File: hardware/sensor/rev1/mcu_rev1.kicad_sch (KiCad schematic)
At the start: 21 parts, among them IC1 STM8L051F3P6, J1 22-28-4044, J2 M20-9770342

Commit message: EG-49 Takachi PCB format.
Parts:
- removed LED3: TLHR4400-AS12Z, MyParts:TLHR4400AS12Z, symbol TLHR4400-AS12Z:TLHR4400-AS12Z
- removed S1, S3: MASM-14R-8-10, MyParts:MASM14R810, symbol MASM-14R-8-10:MASM-14R-8-10
- removed S2: TL6120DF160QG, MyParts:TL6120DF160QG, symbol TL6120DF160QG:TL6120DF160QG
- added LED1: APTD1608LSURCK, MyParts:LEDM168X95N, symbol APTD1608LSURCK:APTD1608LSURCK
- added S1, S3: GP560_20-25, MyParts:GP5602025, symbol GP560_20-25:GP560_20-25
- added S2: PTS636SMG25JSMTR_LFS, MyParts:PTS636SMG25JSMTRLFS, symbol PTS636SMG25JSMTR_LFS:PTS636SMG25JSMTR_LFS
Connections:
- net BTN: now also S2.1 (COM)
- net GND: now also LED1.1 (K), S1.1, S2.2 (NO), S3.1
- net at R2.1, R3.1: now also S1.2, S3.2
- net at R10.2: now also LED1.2 (A)
- no-connect marks 0 -> 2
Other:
- moved on the sheet: R4

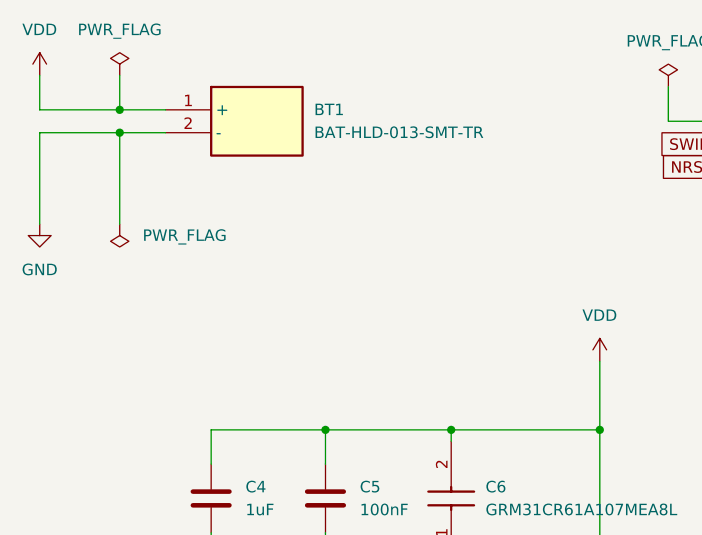
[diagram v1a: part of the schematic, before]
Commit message: EG-49 CST2032 concluded and placed.
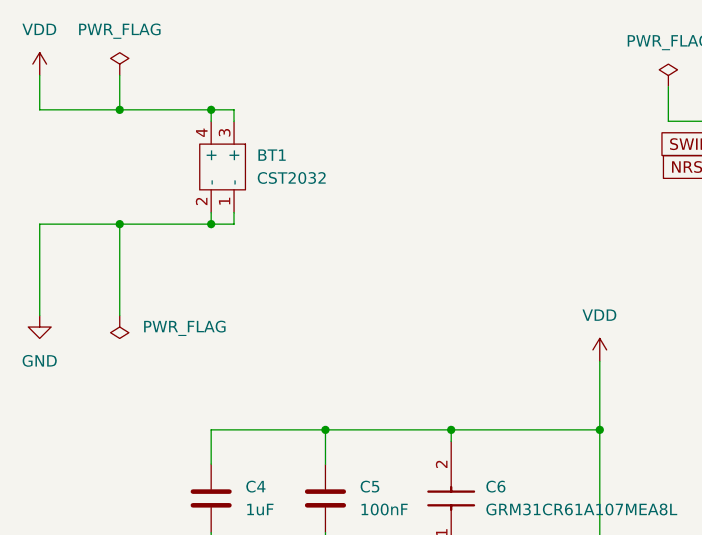
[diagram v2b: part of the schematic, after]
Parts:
- removed BT1: BAT-HLD-013-SMT-TR, MyParts:BATHLD013SMTTR, symbol BAT-HLD-013-SMT-TR:BAT-HLD-013-SMT-TR
- added BT1: CST2032, MyParts:CST2032, symbol CST2032:CST2032
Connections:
- net GND: now also BT1.1 (-), BT1.2 (-)
- net VDD: now also BT1.3 (+), BT1.4 (+)
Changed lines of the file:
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@@
 	)
 	(junction
-		(at 26.67 26.67)
+		(at 26.67 36.83)
 		(diameter 0)
 		(color 0 0 0 0)
@@
 	)
 	(junction
+		(at 36.83 36.83)
+		(diameter 0)
+		(color 0 0 0 0)
+	)
+	(junction
+		(at 36.83 24.13)
+		(diameter 0)
+		(color 0 0 0 0)
+	)
+	(junction
 		(at 134.62 111.76)
 		(diameter 0)
@@
 	(wire
 		(pts
-			(xy 26.67 36.83) (xy 26.67 26.67)
+			(xy 26.67 46.99) (xy 26.67 36.83)
 		)
 		(stroke
@@
 	(wire
 		(pts
+			(xy 39.37 36.83) (xy 39.37 35.56)
+		)
+		(stroke
+			(width 0)
+			(type default)
+		)
+	)
+	(wire
+		(pts
 			(xy 46.99 167.64) (xy 46.99 171.45)
 		)
@@
 	(wire
 		(pts
-			(xy 26.67 26.67) (xy 31.75 26.67)
+			(xy 26.67 36.83) (xy 36.83 36.83)
 		)
 		(stroke
@@
 	(wire
 		(pts
-			(xy 17.78 26.67) (xy 17.78 36.83)
+			(xy 17.78 36.83) (xy 17.78 46.99)
 		)
 		(stroke
@@
 	(wire
 		(pts
+			(xy 36.83 36.83) (xy 36.83 35.56)
+		)
+		(stroke
+			(width 0)
+			(type default)
+		)
+	)
+	(wire
+		(pts
 			(xy 100.33 33.02) (xy 96.52 33.02)
 		)
@@
 	(wire
 		(pts
+			(xy 36.83 24.13) (xy 39.37 24.13)
+		)
+		(stroke
+			(width 0)
+			(type default)
+		)
+	)
+	(wire
+		(pts
 			(xy 46.99 157.48) (xy 46.99 160.02)
 		)
@@
 	(wire
 		(pts
+			(xy 36.83 24.13) (xy 36.83 25.4)
+		)
+		(stroke
+			(width 0)
+			(type default)
+		)
+	)
+	(wire
+		(pts
 			(xy 125.73 96.52) (xy 143.51 96.52)
 		)
@@
 	(wire
 		(pts
+			(xy 36.83 36.83) (xy 39.37 36.83)
+		)
+		(stroke
+			(width 0)
+			(type default)
+		)
+	)
+	(wire
+		(pts
 			(xy 140.97 161.29) (xy 147.32 161.29)
 		)
@@
 	(wire
 		(pts
+			(xy 39.37 24.13) (xy 39.37 25.4)
+		)
+		(stroke
+			(width 0)
+			(type default)
+		)
+	)
+	(wire
+		(pts
 			(xy 36.83 59.69) (xy 36.83 63.5)
 		)
@@
 	(wire
 		(pts
-			(xy 26.67 26.67) (xy 17.78 26.67)
+			(xy 26.67 36.83) (xy 17.78 36.83)
 		)
 		(stroke
@@
 	(wire
 		(pts
-			(xy 26.67 24.13) (xy 31.75 24.13)
+			(xy 26.67 24.13) (xy 36.83 24.13)
 		)
 		(stroke
@@
 	)
 	(symbol
-		(lib_id "BAT-HLD-013-SMT-TR:BAT-HLD-013-SMT-TR")
-		(at 31.75 24.13 0)
-		(unit 1)
-		(exclude_from_sim no)
-		(in_bom yes)
-		(on_board yes)
-		(dnp no)
-		(fields_autoplaced yes)
-		(property "Reference" "BT1"
-			(at 48.26 24.1299 0)
-			(effects
-				(font
-					(size 1.27 1.27)
-				)
-				(justify left)
-			)
-		)
-		(property "Value" "BAT-HLD-013-SMT-TR"
-			(at 48.26 26.6699 0)
-			(effects
-				(font
-					(size 1.27 1.27)
-				)
-				(justify left)
-			)
-		)
-		(property "Footprint" "MyParts:BATHLD013SMTTR"
-			(at 48.26 119.05 0)
-			(effects
-				(font
-					(size 1.27 1.27)
-				)
-				(justify left top)
-				(hide yes)
-			)
-		)
-		(property "Datasheet" "https://www.te.com/en/product-BAT-HLD-013-SMT-TR.html"
-			(at 48.26 219.05 0)
-			(effects
-				(font
-					(size 1.27 1.27)
-				)
-				(justify left top)
-				(hide yes)
-			)
-		)
-		(property "Description" "CR2032 Battery Holder, 1 Position, Horizontal, Nickel (Ni)"
-			(at 31.75 24.13 0)
-			(effects
-				(font
-					(size 1.27 1.27)
-				)
-				(hide yes)
-			)
-		)
-		(property "Height" "6.5"
-			(at 48.26 419.05 0)
-			(effects
-				(font
-					(size 1.27 1.27)
-				)
-				(justify left top)
-				(hide yes)
-			)
-		)
-		(property "Mouser Part Number" "712-BAT-HLD-013SMTTR"
-			(at 48.26 519.05 0)
-			(effects
-				(font
-					(size 1.27 1.27)
-				)
-				(justify left top)
-				(hide yes)
-			)
-		)
-		(property "Mouser Price/Stock" "https://www.mouser.co.uk/ProductDetail/TE-Connectivity-Linx-Technologies/BAT-HLD-013-SMT-TR?qs=4ASt3YYao0UKhYWrBts7tw%3D%3D"
-			(at 48.26 619.05 0)
-			(effects
-				(font
-					(size 1.27 1.27)
-				)
-				(justify left top)
-				(hide yes)
-			)
-		)
-		(property "Manufacturer_Name" "TE Connectivity"
-			(at 48.26 719.05 0)
-			(effects
-				(font
-					(size 1.27 1.27)
-				)
-				(justify left top)
-				(hide yes)
-			)
-		)
-		(property "Manufacturer_Part_Number" "BAT-HLD-013-SMT-TR"
-			(at 48.26 819.05 0)
-			(effects
-				(font
-					(size 1.27 1.27)
-				)
-				(justify left top)
-				(hide yes)
-			)
-		)
-		(pin "2"
-		)
-		(pin "1"
-		)
-		(instances
-			(project ""
-				(path "/c9ab58dc-163d-4c4e-8d12-3a07665777cf"
-					(reference "BT1")
-					(unit 1)
-				)
-			)
-			(project "sensor_rev1"
-				(path "/d3cb7130-decc-418b-958e-e5d84a8d867f/ec220677-d66d-4ee1-961f-1c93fb46783a"
-					(reference "BT1")
-					(unit 1)
-				)
-			)
-		)
-	)
-	(symbol
 		(lib_id "Device:R_US")
 		(at 157.48 147.32 90)
@@
 	)
 	(symbol
+		(lib_id "CST2032:CST2032")
+		(at 38.1 30.48 270)
+		(unit 1)
+		(exclude_from_sim no)
+		(in_bom yes)
+		(on_board yes)
+		(dnp no)
+		(fields_autoplaced yes)
+		(property "Reference" "BT1"
+			(at 41.91 29.2099 90)
+			(effects
+				(font
+					(size 1.27 1.27)
+				)
+				(justify left)
+			)
+		)
+		(property "Value" "CST2032"
+			(at 41.91 31.7499 90)
+			(effects
+				(font
+					(size 1.27 1.27)
+				)
+				(justify left)
+			)
+		)
+		(property "Footprint" "MyParts:CST2032"
+			(at 38.1 30.48 0)
+			(effects
+				(font
+					(size 1.27 1.27)
+				)
+				(hide yes)
+			)
+		)
+		(property "Datasheet" ""
+			(at 38.1 30.48 0)
+			(effects
+				(font
+					(size 1.27 1.27)
+				)
+				(hide yes)
+			)
+		)
+		(property "Description" ""
+			(at 38.1 30.48 0)
+			(effects
+				(font
+					(size 1.27 1.27)
+				)
+				(hide yes)
+			)
+		)
+		(pin "2"
+		)
+		(pin "3"
+		)
+		(pin "1"
+		)
+		(pin "4"
+		)
+		(instances
+			(project ""
+				(path "/d3cb7130-decc-418b-958e-e5d84a8d867f/ec220677-d66d-4ee1-961f-1c93fb46783a"
+					(reference "BT1")
+					(unit 1)
+				)
+			)
+		)
+	)
+	(symbol
 		(lib_id "Device:R_US")
 		(at 39.37 157.48 90)
@@
 	(symbol
 		(lib_id "power:PWR_FLAG")
-		(at 26.67 36.83 180)
+		(at 26.67 46.99 180)
 		(unit 1)
 		(exclude_from_sim no)
@@
 		(fields_autoplaced yes)
 		(property "Reference" "#FLG02"
-			(at 26.67 38.735 0)
+			(at 26.67 48.895 0)
 			(effects
 				(font
@@
 		)
 		(property "Value" "PWR_FLAG"
-			(at 29.21 38.0999 0)
+			(at 29.21 48.2599 0)
 			(effects
 				(font
@@
 		)
 		(property "Footprint" ""
-			(at 26.67 36.83 0)
+			(at 26.67 46.99 0)
 			(effects
 				(font
@@
 		)
 		(property "Datasheet" "~"
-			(at 26.67 36.83 0)
+			(at 26.67 46.99 0)
 			(effects
 				(font
@@
 		)
 		(property "Description" "Special symbol for telling ERC where power comes from"
-			(at 26.67 36.83 0)
+			(at 26.67 46.99 0)
 			(effects
 				(font
@@
 	(symbol
 		(lib_id "power:GND")
-		(at 17.78 36.83 0)
+		(at 17.78 46.99 0)
 		(unit 1)
 		(exclude_from_sim no)
@@
 		(fields_autoplaced yes)
 		(property "Reference" "#PWR019"
-			(at 17.78 43.18 0)
+			(at 17.78 53.34 0)
 			(effects
 				(font
@@
 		)
 		(property "Value" "GND"
-			(at 17.78 41.91 0)
+			(at 17.78 52.07 0)
 			(effects
 				(font
@@
 		)
 		(property "Footprint" ""
-			(at 17.78 36.83 0)
+			(at 17.78 46.99 0)
 			(effects
 				(font
@@
 		)
 		(property "Datasheet" ""
-			(at 17.78 36.83 0)
+			(at 17.78 46.99 0)
 			(effects
 				(font
@@
 		)
 		(property "Description" "Power symbol creates a global label with name \"GND\" , ground"
-			(at 17.78 36.83 0)
+			(at 17.78 46.99 0)
 			(effects
 				(font

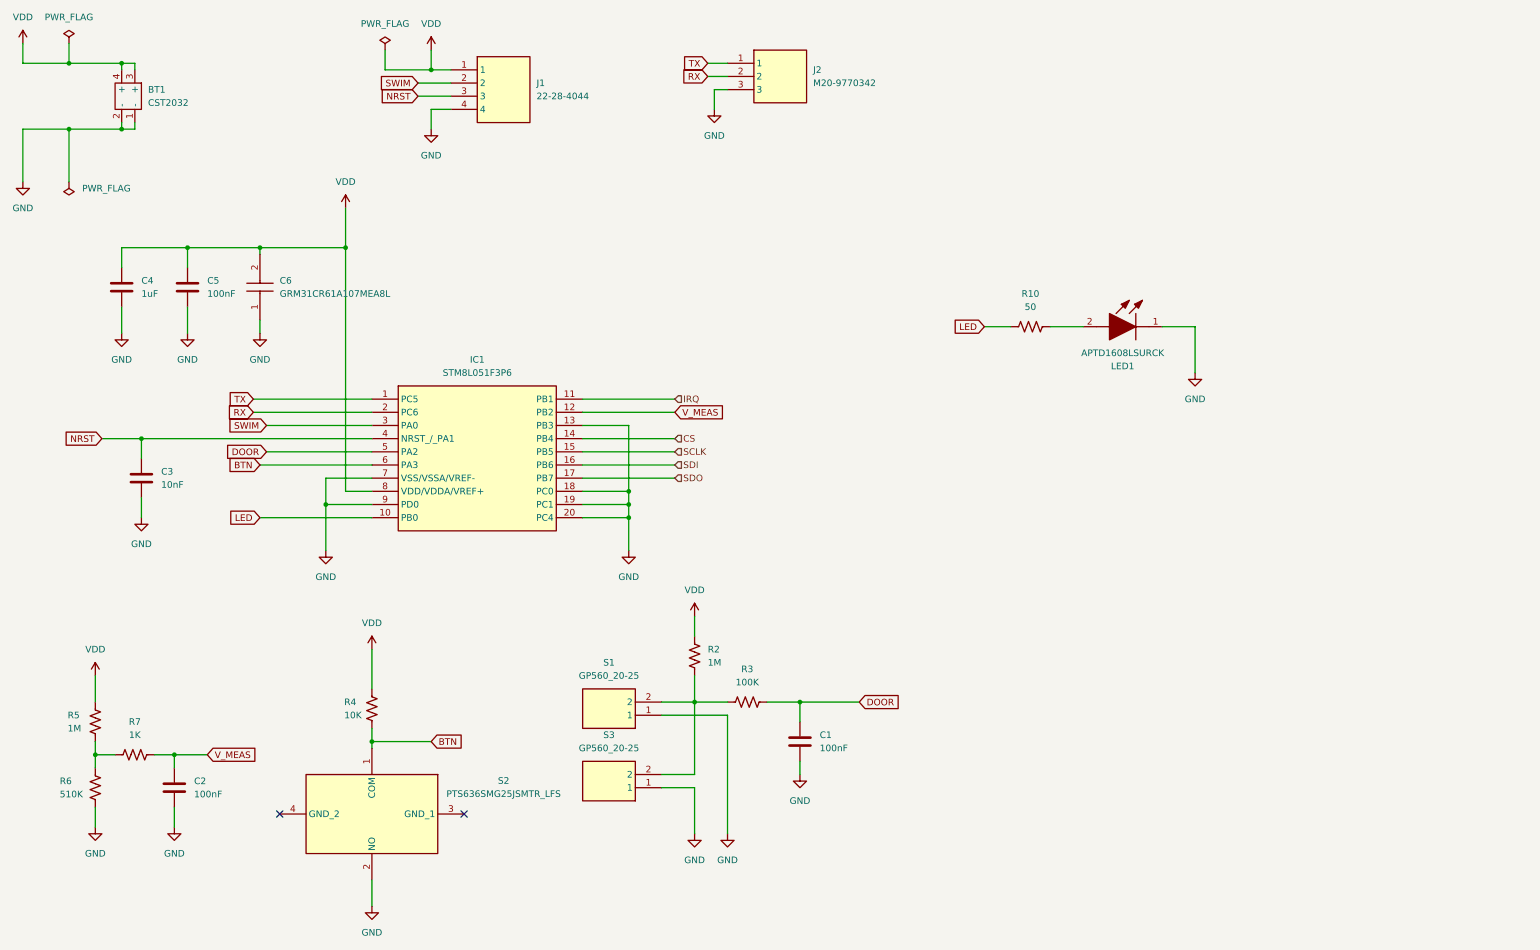
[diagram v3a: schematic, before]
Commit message: EG-49 Removed a bulk capacitor.
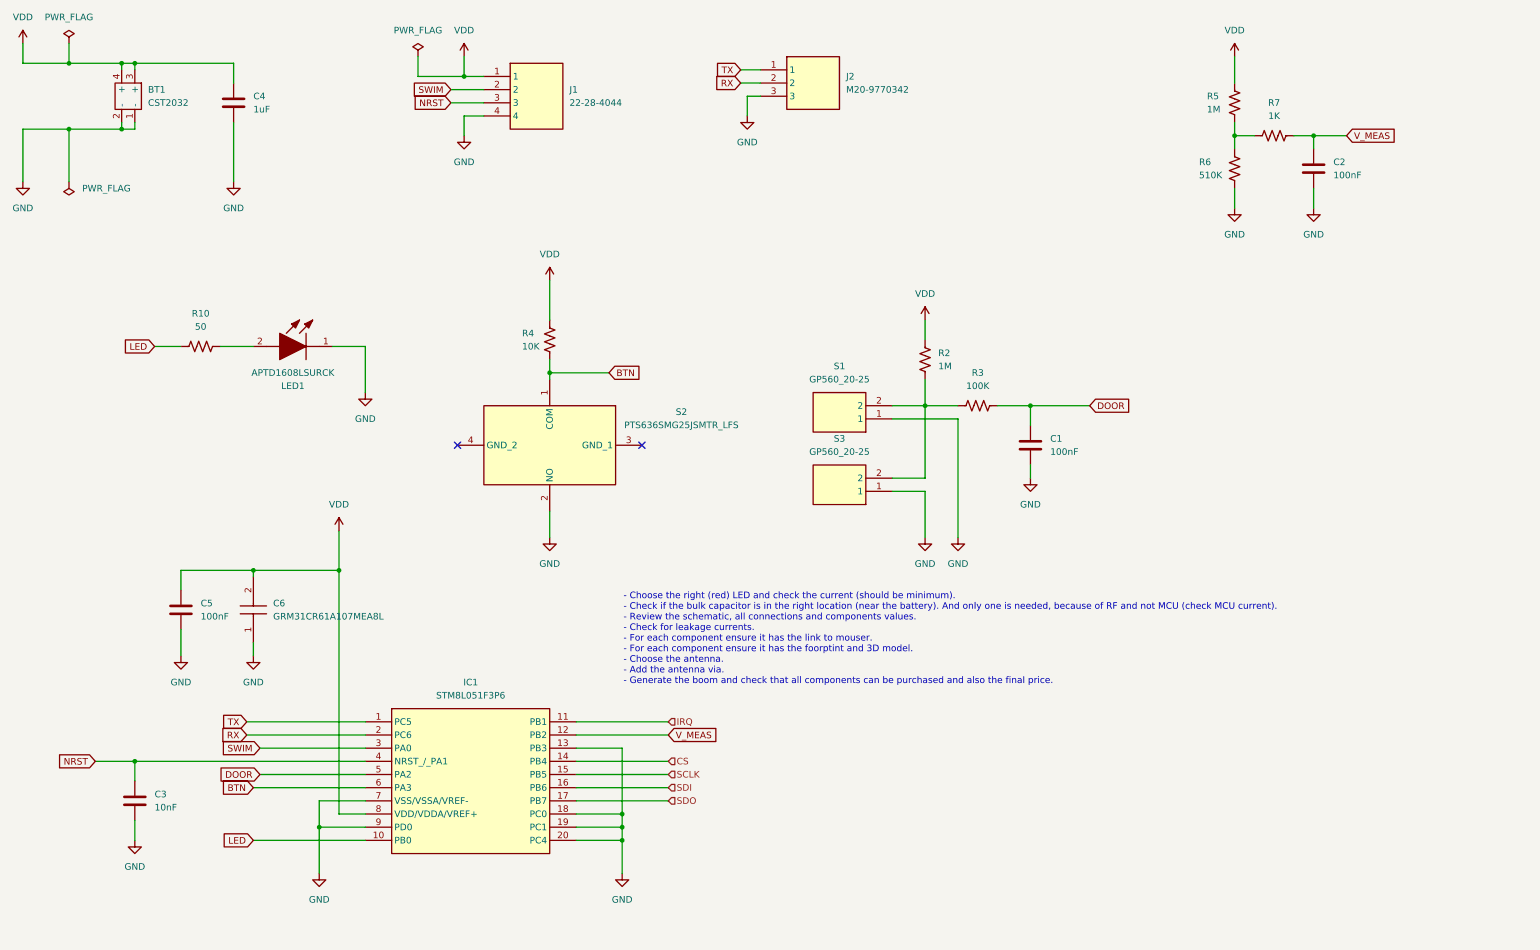
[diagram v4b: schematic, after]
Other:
- note added: "- Choose the right (red) LED and check the current (should be minimum). - Check if the bulk capacitor is in the right location (near the battery). And only one is needed, because of RF and not MCU (check MCU current). - Review the schematic, all connections and components values. - Check for leakage currents. - For each component ensure it has the link to mouser. - For each component ensure it ha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"
- moved on the sheet: C1, C2, C3, C4, C5, C6, IC1, J1, J2, LED1, R10, R2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

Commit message: EG-49 MCU schematic part is concluded.
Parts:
- removed C4: 1uF, Capacitor_SMD:C_0402_1005Metric, symbol Device:C
- removed LED1: APTD1608LSURCK, MyParts:LEDM168X95N, symbol APTD1608LSURCK:APTD1608LSURCK
- added LED1: VLMS3000-GS08, MyParts:VLMS3000GS08, symbol VLMS3000-GS08:VLMS3000-GS08
- C2: renamed from C1; footprint Capacitor_SMD:C_0402_1005Metric -> Capacitor_SMD:C_0603_1608Metric
- C3: renamed from C2; footprint Capacitor_SMD:C_0402_1005Metric -> Capacitor_SMD:C_0603_1608Metric
- C4: renamed from C5; footprint Capacitor_SMD:C_0402_1005Metric -> Capacitor_SMD:C_0603_1608Metric
- C5: renamed from C3; footprint Capacitor_SMD:C_0402_1005Metric -> Capacitor_SMD:C_0603_1608Metric
- R1: renamed from R10; value 50 -> 100; footprint Resistor_SMD:R_0402_1005Metric -> Resistor_SMD:R_0603_1608Metric
- R2: renamed from R4; footprint Resistor_SMD:R_0402_1005Metric -> Resistor_SMD:R_0603_1608Metric
- R3: renamed from R2; footprint Resistor_SMD:R_0402_1005Metric -> Resistor_SMD:R_0603_1608Metric
- R4: renamed from R3; footprint Resistor_SMD:R_0402_1005Metric -> Resistor_SMD:R_0603_1608Metric
- R5: footprint Resistor_SMD:R_0402_1005Metric -> Resistor_SMD:R_0603_1608Metric
- R6: renamed from R7; footprint Resistor_SMD:R_0402_1005Metric -> Resistor_SMD:R_0603_1608Metric
- R7: renamed from R6; footprint Resistor_SMD:R_0402_1005Metric -> Resistor_SMD:R_0603_1608Metric
- renumbered C6 to C1, S3 to S2, S2 to S3
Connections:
- net GND: now also LED1.1 (K)
- net at R1.2: now also LED1.2 (A)
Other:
- note added: "- Check if the bulk capacitor is in the right location (near the battery). And only one is needed, because of RF and not MCU (check MCU current). - Review the schematic, all connections and components values. - Check for leakage currents. - For each component ensure it has the link to mouser. - For each component ensure it has the foorptint and 3D model. - Choose the antenna. - Add the antenna vi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"
- note removed: "- Choose the right (red) LED and check the current (should be minimum). - Check if the bulk capacitor is in the right location (near the battery). And only one is needed, because of RF and not MCU (check MCU current). - Review the schematic, all connections and components values. - Check for leakage currents. - For each component ensure it has the link to mouser. - For each component ensure it ha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"
- moved on the sheet: C1, C4

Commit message: EG-49 All components from MCU schematic with links to supplier.
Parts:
- C2: renamed from C3; Manufacturer Yageo -> Wurth Elektronic; Manufacturer Part Number CC0402KRX7R7BB104 -> 885012206020; Mouser Part Number 603-CC402KRX7R7BB104 -> 710-885012206020; Supplier Link https://pt.mouser.com/ProductDetail/YAGEO/CC0402KRX7R7BB104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 -> https://pt.mouser.com/en/ProductDetail/Wurth-Elektronik/885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
- C3: renamed from C2; Manufacturer Yageo -> Wurth Elektronik; Manufacturer Part Number CC0402KRX7R7BB104 -> 885012206020; Mouser Part Number 603-CC402KRX7R7BB104 -> 710-885012206020; Supplier Link https://pt.mouser.com/ProductDetail/YAGEO/CC0402KRX7R7BB104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 -> https://pt.mouser.com/en/ProductDetail/Wurth-Elektronik/885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
- C4: Manufacturer Yageo -> Wurth Elektronik; Manufacturer Part Number CC0402KRX7R7BB104 -> 885012206020; Mouser Part Number 603-CC402KRX7R7BB104 -> 710-885012206020; Supplier Link https://pt.mouser.com/ProductDetail/YAGEO/CC0402KRX7R7BB104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 -> https://pt.mouser.com/en/ProductDetail/Wurth-Elektronik/885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
- C5: Manufacturer Murata -> YAGEO; Manufacturer Part Number GXT155R71C103KE01D -> CC0603KRX7R6BB103; Mouser Part Number 81-GXT155R71C103KE1D -> 603-CC603KRX7R6BB103; Supplier Link https://pt.mouser.com/ProductDetail/Murata-Electronics/GXT1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 -> https://pt.mouser.com/en/ProductDetail/YAGEO/CC0603KRX7R6BB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
- J1: Mouser Price/Stock https://www.mouser.com/Search/Refine.aspx?Keyword=538-22-28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 -> https://pt.mouser.com/en/ProductDetail/Molex/22-28-4044?qs=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
- R1: Manufacturer Part Number AC0402JR-0750RL -> RC0603JR-13100RL; Mouser Part Number 603-AC0402JR-0750RL -> 603-RC0603JR-13100RL; Supplier Link https://pt.mouser.com/ProductDetail/YAGEO/AC0402JR-0750RL?q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 -> https://pt.mouser.com/en/ProductDetail/YAGEO/RC0603JR-13100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
- R2: renamed from R3; Manufacturer Panasonic -> Yageo; Manufacturer Part Number ERJ-2RKD1004X -> RC0603JR-101ML; Mouser Part Number 667-ERJ-2RKD1004X -> 603-RC0603JR-101ML; Supplier Link https://pt.mouser.com/ProductDetail/Panasonic/ERJ-2RKD1004X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 -> https://pt.mouser.com/en/ProductDetail/YAGEO/RC0603JR-101ML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
- R3: renamed from R4; Manufacturer Yageo -> Vishay; Manufacturer Part Number RC0402JR-7D100KL -> CRCW0603100KJNEAC; Mouser Part Number 603-RC0402JR-7D100KL -> 71-CRCW0603100KJNEAC; Supplier Link https://pt.mouser.com/ProductDetail/YAGEO/RC0402JR-7D100KL?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 -> https://pt.mouser.com/en/ProductDetail/Vishay/CRCW0603100KJ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
- R4: renamed from R2; Manufacturer Panasonic -> Vishay; Manufacturer Part Number AC0402JR-7D10KL -> CRCW060310K0JNEBC; Mouser Part Number 603-AC0402JR-7D10KL -> 71-CRCW060310K0JNEBC; Supplier Link https://pt.mouser.com/ProductDetail/YAGEO/AC0402JR-7D10KL?q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 -> https://pt.mouser.com/en/ProductDetail/Vishay/CRCW060310K0J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
- R5: Manufacturer Panasonic -> Yageo; Manufacturer Part Number ERJ-2RKD1004X -> RC0603JR-101ML; Mouser Part Number 667-ERJ-2RKD1004X -> 603-RC0603JR-101ML; Supplier Link https://pt.mouser.com/ProductDetail/Panasonic/ERJ-2RKD1004X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 -> https://pt.mouser.com/en/ProductDetail/YAGEO/RC0603JR-101ML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
- R6: renamed from R7; Manufacturer Part Number ERJ-2RKD5103X -> ERJ-3GEYJ514V; Mouser Part Number 667-ERJ-2RKD5103X -> 667-ERJ-3GEYJ514V; Supplier Link https://pt.mouser.com/ProductDetail/Panasonic/ERJ-2RKD5103X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 -> https://pt.mouser.com/en/ProductDetail/Panasonic/ERJ-3GEYJ5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
- R7: renamed from R6; Manufacturer Part Number RC0402JR-7D1KL -> 603-RC0603JR-7W1KL; Mouser Part Number 603-RC0402JR-7D1KL -> 603-RC0603JR-7W1KL; Supplier Link https://pt.mouser.com/ProductDetail/YAGEO/RC0402JR-7D1KL?qs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 -> https://pt.mouser.com/en/ProductDetail/YAGEO/RC0603JR-7W1KL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
- renumbered S3 to S2, S2 to S3
